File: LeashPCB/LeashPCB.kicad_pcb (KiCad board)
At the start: 2 copper layers, 40 x 30 mm, 0 parts

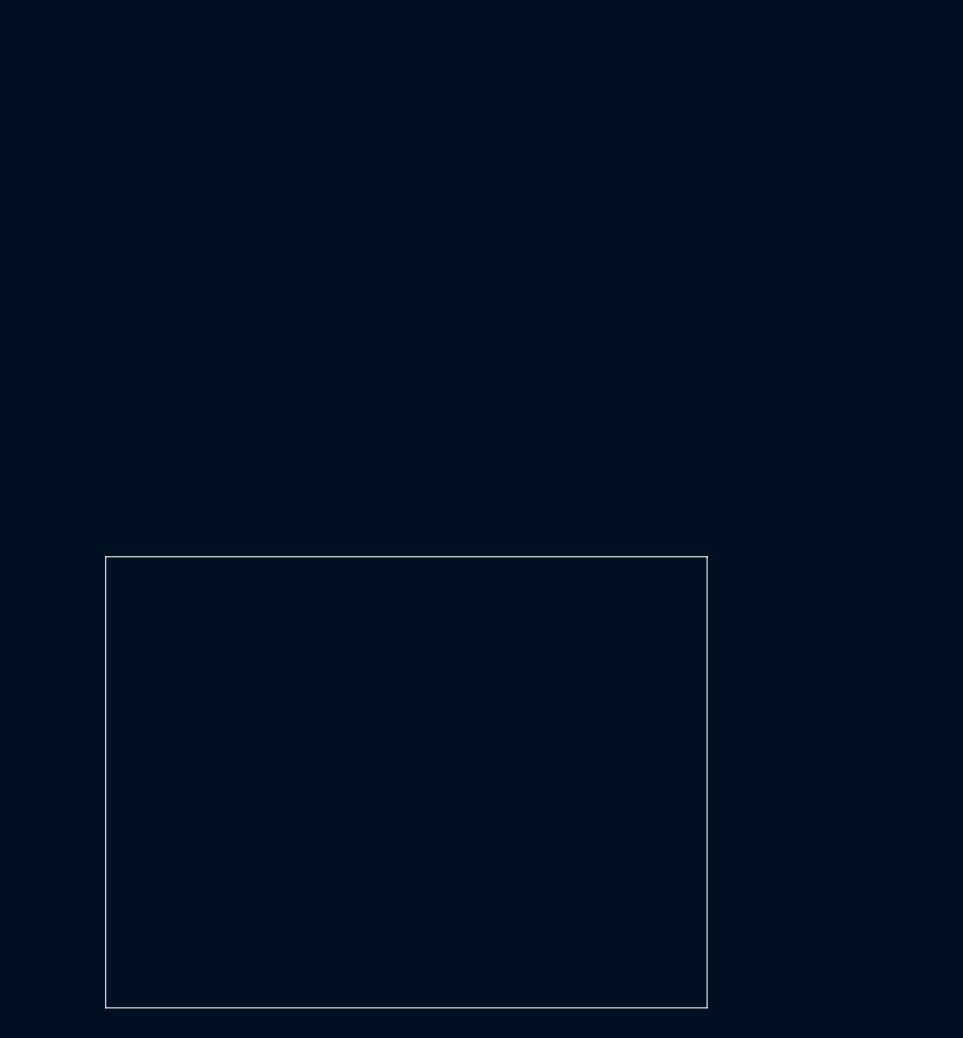
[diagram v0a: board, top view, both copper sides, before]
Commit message: Started adding battery holder info (built ins)
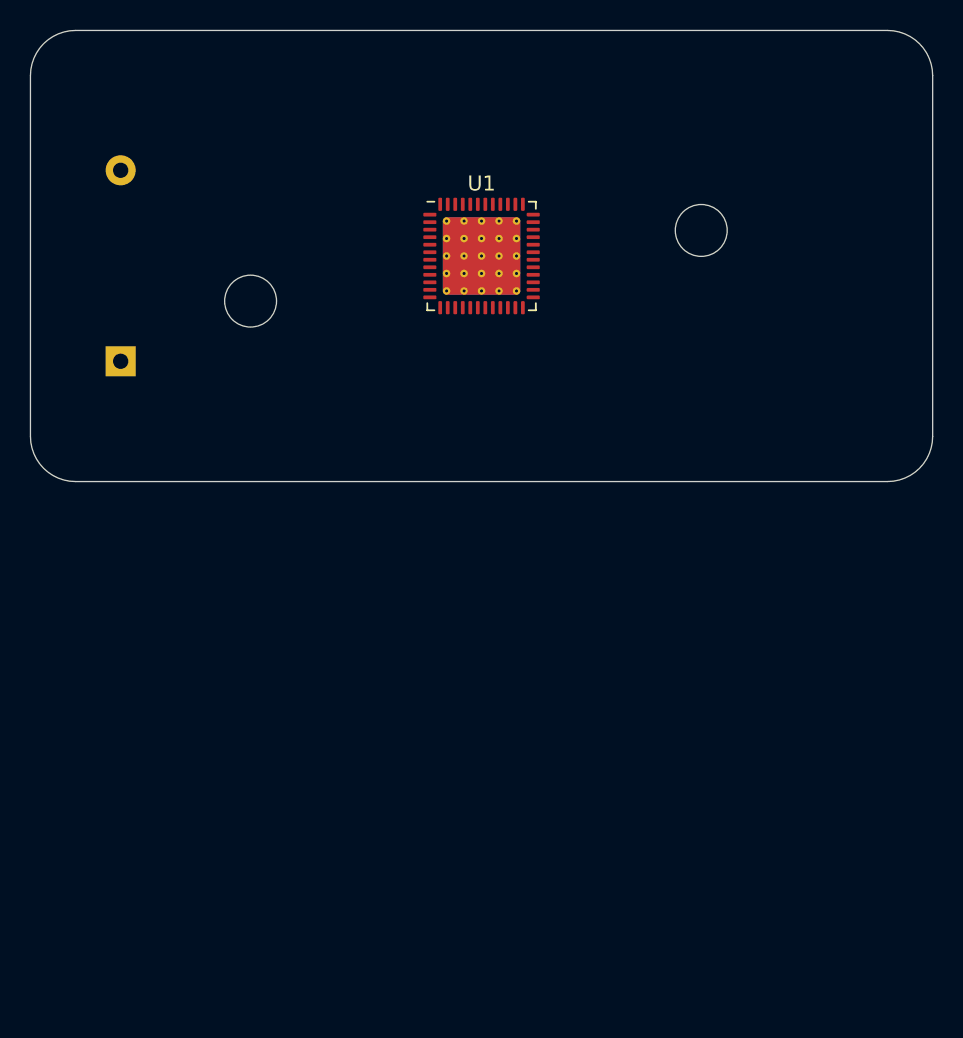
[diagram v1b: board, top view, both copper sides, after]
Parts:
- added BT1: Battery, Battery:BatteryHolder_Keystone_2468_2xAAA, B.Cu at (106.0, 72.0)
- added U1: CC1352R, Package_DFN_QFN:QFN-48-1EP_7x7mm_P0.5mm_EP5.15x5.15mm_ThermalVias, F.Cu at (130.0, 65.0)
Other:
- board size 40 x 30 mm -> 60 x 30 mm
